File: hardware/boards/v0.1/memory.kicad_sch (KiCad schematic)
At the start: 10 parts, among them IC1 W25Q512JVEIQ, IC4 IS42S16160J-7TLI, J3 MICRO_SD

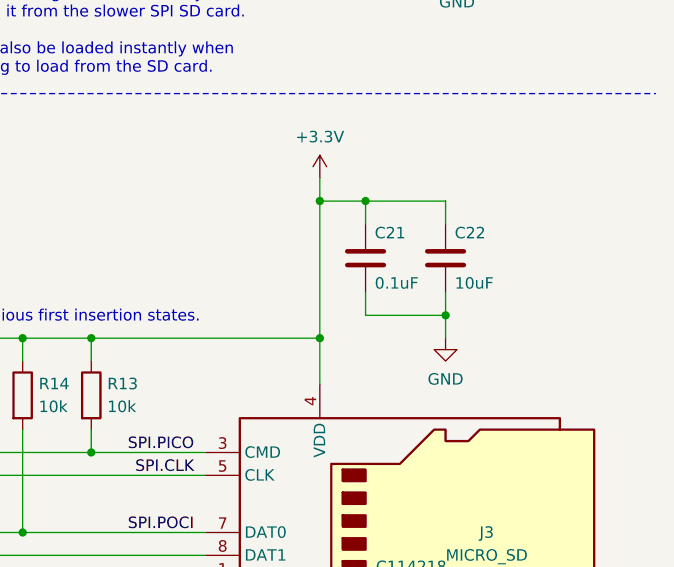
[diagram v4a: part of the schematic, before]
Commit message: feat: routing cleanup and start of BOM selection
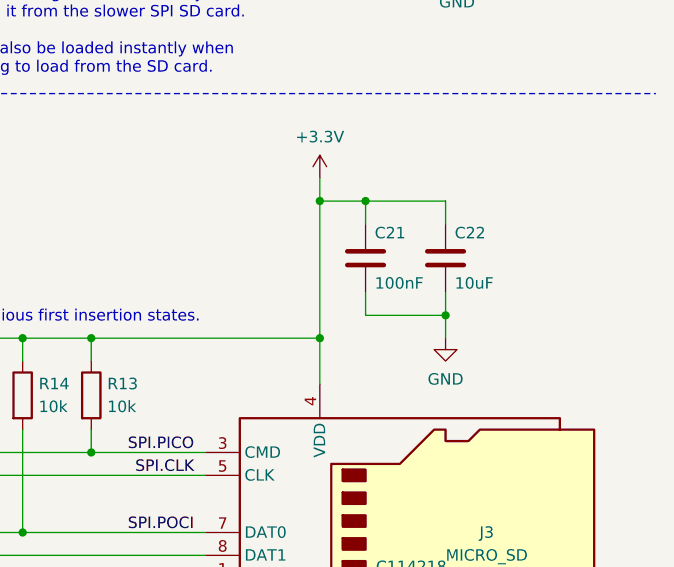
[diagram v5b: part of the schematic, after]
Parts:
- C21: value 0.1uF -> 100nF; JLC (none) -> C1525
- C22: JLC (none) -> C15525
- IC1: JLC C7389628 -> C2986165
- IC4: JLC (none) -> C412833
- R13, R14, R15, R16, R17: JLC (none) -> C25531
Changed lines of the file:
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@@
 		(polyline
 			(pts
-				(xy 121.92 81.28) (xy 121.92 101.6) (xy 134.62 101.6) (xy 134.62 81.28)
+				(xy 121.92 81.28) (xy 121.92 59.69) (xy 134.62 59.69) (xy 134.62 81.28)
 			)
 			(stroke
@@
 		(polyline
 			(pts
-				(xy 121.92 81.28) (xy 121.92 59.69) (xy 134.62 59.69) (xy 134.62 81.28)
+				(xy 121.92 81.28) (xy 121.92 101.6) (xy 134.62 101.6) (xy 134.62 81.28)
 			)
 			(stroke
@@
 			)
 		)
+		(property "JLC" "C25531"
+			(at 207.01 109.22 0)
+			(effects
+				(font
+					(size 1.27 1.27)
+				)
+				(hide yes)
+			)
+		)
 		(pin "1"
 		)
@@
 			)
 		)
-		(property "Value" "0.1uF"
+		(property "Value" "100nF"
 			(at 253.746 96.774 0)
 			(effects
@@
 					(size 1.27 1.27)
 				)
+			)
+		)
+		(property "JLC" "C1525"
+			(at 252.73 93.98 0)
+			(effects
+				(font
+					(size 1.27 1.27)
+				)
+				(hide yes)
 			)
 		)
@@
 			)
 		)
-		(property "JLC" "C7389628"
+		(property "JLC" "C2986165"
 			(at 262.89 41.91 0)
 			(effects
@@
 			)
 		)
+		(property "JLC" "C25531"
+			(at 191.77 109.22 0)
+			(effects
+				(font
+					(size 1.27 1.27)
+				)
+				(hide yes)
+			)
+		)
 		(pin "1"
 		)
@@
 			)
 		)
+		(property "JLC" "C25531"
+			(at 214.63 109.22 0)
+			(effects
+				(font
+					(size 1.27 1.27)
+				)
+				(hide yes)
+			)
+		)
 		(pin "1"
 		)
@@
 			)
 		)
+		(property "JLC" "C25531"
+			(at 199.39 109.22 0)
+			(effects
+				(font
+					(size 1.27 1.27)
+				)
+				(hide yes)
+			)
+		)
 		(pin "1"
 		)
@@
 			)
 		)
+		(property "JLC" "C412833"
+			(at 105.41 93.98 0)
+			(effects
+				(font
+					(size 1.27 1.27)
+				)
+				(hide yes)
+			)
+		)
 		(pin "49"
 		)
@@
 					(size 1.27 1.27)
 				)
+			)
+		)
+		(property "JLC" "C15525"
+			(at 261.62 93.98 0)
+			(effects
+				(font
+					(size 1.27 1.27)
+				)
+				(hide yes)
 			)
 		)
@@
 			)
 		)
+		(property "JLC" "C25531"
+			(at 222.25 109.22 0)
+			(effects
+				(font
+					(size 1.27 1.27)
+				)
+				(hide yes)
+			)
+		)

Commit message: feat: update various components to 0402
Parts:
- IC1: Mouser Part Number 454-W25Q512JVEIQ -> (none); Mouser Price/Stock https://www.mouser.co.uk/ProductDetail/Winbond/W25Q512JVEIQ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 -> (none)
- IC4: Mouser Part Number 870-IS42S16160J-7TLI -> (none); Mouser Price/Stock https://www.mouser.co.uk/ProductDetail/ISSI/IS42S16160J-7TL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 -> (none)

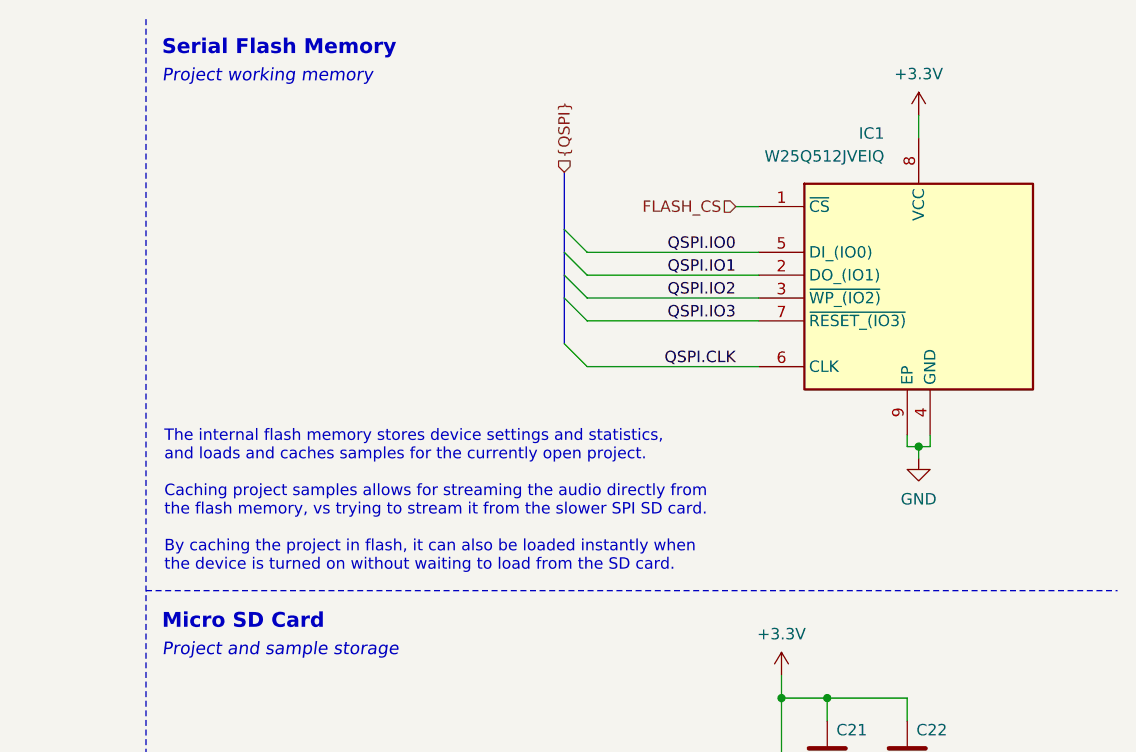
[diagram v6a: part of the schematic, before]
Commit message: feat: various routing cleanup, add SD flash
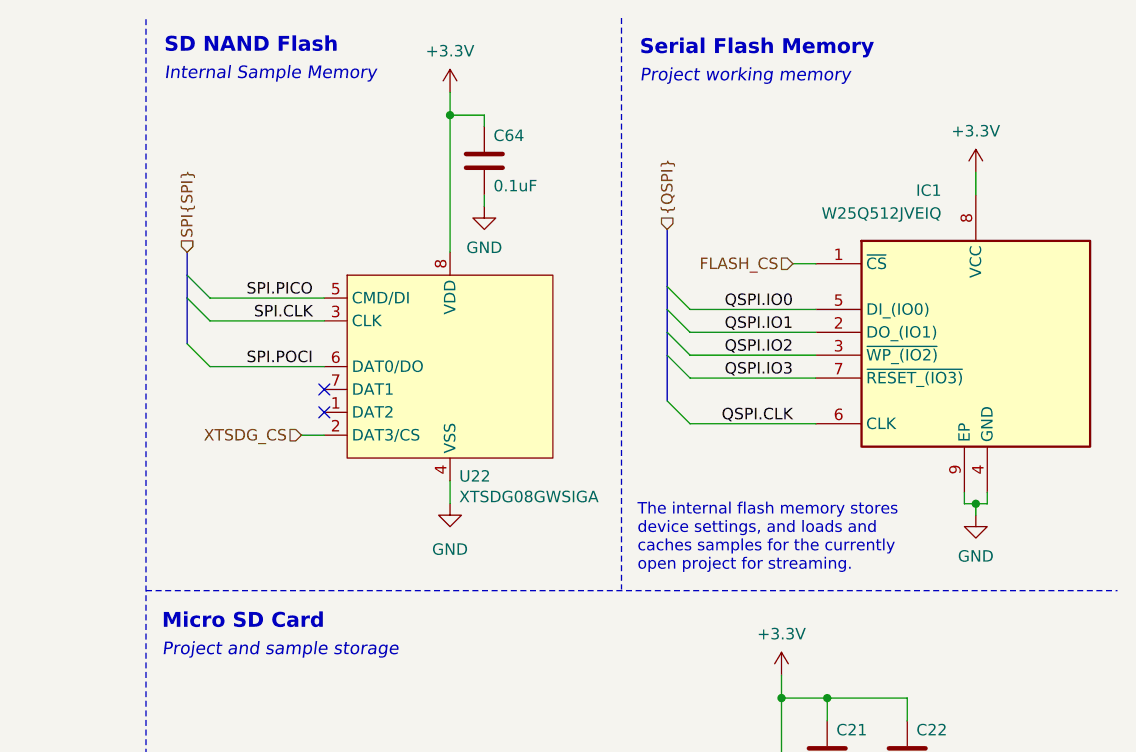
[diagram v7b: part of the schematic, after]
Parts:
- added C64: 0.1uF, Capacitor_SMD:C_0402_1005Metric, symbol Device:C
- added U22: XTSDG08GWSIGA, Package_SON:WSON-8-1EP_8x6mm_P1.27mm_EP3.4x4.3mm, symbol pocket_synth:XTSDG08GWSIGA
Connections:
- net +3.3V: now also C64.1, U22.8 (VDD)
- net GND: now also C64.2, U22.4 (VSS)
- net SPI.CLK: now also U22.3 (CLK)
- net SPI.PICO: now also U22.5 (CMD/DI)
- net SPI.POCI: now also U22.6 (DAT0/DO)
- new net XTSDG_CS: U22.2 (DAT3/CS)
- no-connect marks 2 -> 4
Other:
- note added: "Internal Sample Memory"
- note added: "SD NAND Flash"
- note added: "The internal flash memory stores device settings, and loads and caches samples for the currently open project for streaming."
- note removed: "The internal flash memory stores device settings and statistics, and loads and caches samples for the currently open project. Caching project samples allows for streaming the audio directly from the flash memory, vs trying to stream it from the slower SPI SD card. By caching the project in flash, it can also be loaded instantly when the device is turned on without waiting to load from the SD card."
- moved on the sheet: IC1

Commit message: chore: more schematic and routing organization
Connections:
- net GND: now also U22.9 (EP)
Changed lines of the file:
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@@
 	)
 	(junction
+		(at 210.82 64.77)
+		(diameter 0)
+		(color 0 0 0 0)
+	)
+	(junction
 		(at 247.65 102.87)
 		(diameter 0)
@@
 	(wire
 		(pts
+			(xy 209.55 63.5) (xy 209.55 64.77)
+		)
+		(stroke
+			(width 0)
+			(type default)
+		)
+	)
+	(wire
+		(pts
 			(xy 207.01 102.87) (xy 214.63 102.87)
 		)
@@
 		)
 	)
+	(wire
+		(pts
+			(xy 210.82 64.77) (xy 212.09 64.77)
+		)
+		(stroke
+			(width 0)
+			(type default)
+		)
+	)
 	(bus
 		(pts
@@
 		)
 	)
+	(wire
+		(pts
+			(xy 210.82 64.77) (xy 210.82 66.04)
+		)
+		(stroke
+			(width 0)
+			(type default)
+		)
+	)
 	(bus
 		(pts
@@
 	(wire
 		(pts
+			(xy 212.09 64.77) (xy 212.09 63.5)
+		)
+		(stroke
+			(width 0)
+			(type default)
+		)
+	)
+	(wire
+		(pts
 			(xy 76.2 100.33) (xy 88.9 100.33)
 		)
@@
 		)
 	)
-	(wire
-		(pts
-			(xy 210.82 63.5) (xy 210.82 66.04)
-		)
-		(stroke
-			(width 0)
-			(type default)
-		)
-	)
 	(bus
 		(pts
@@
 	(wire
 		(pts
+			(xy 209.55 64.77) (xy 210.82 64.77)
+		)
+		(stroke
+			(width 0)
+			(type default)
+		)
+	)
+	(wire
+		(pts
 			(xy 76.2 74.93) (xy 88.9 74.93)
 		)
@@
 		(dnp no)
 		(property "Reference" "U22"
-			(at 211.836 62.992 0)
+			(at 213.106 62.738 0)
 			(effects
 				(font
@@
 		)
 		(property "Value" "XTSDG08GWSIGA"
-			(at 211.836 65.278 0)
+			(at 213.106 65.024 0)
 			(effects
 				(font
@@
 		(pin "8"
 		)
+		(pin "9"
+		)
 		(instances
